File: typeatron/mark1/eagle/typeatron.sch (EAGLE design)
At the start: 24 parts

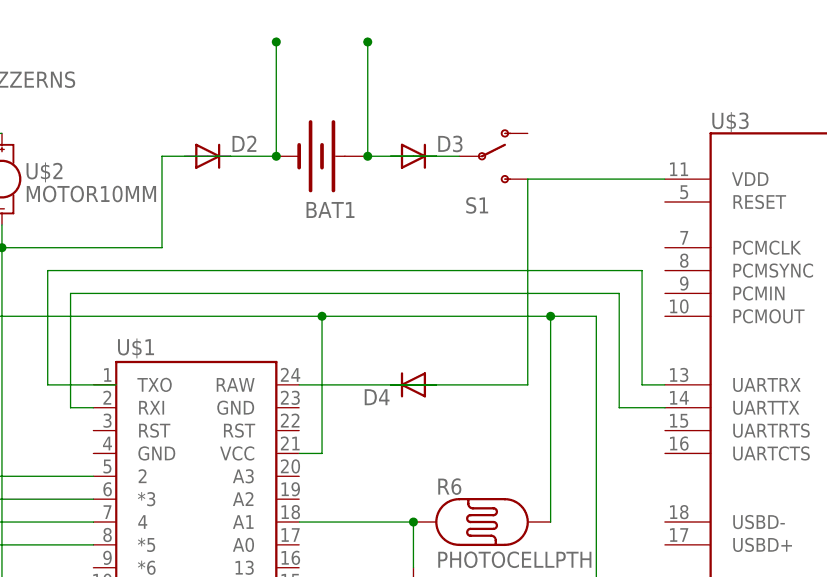
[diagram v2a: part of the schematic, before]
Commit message: Yet another diode revision; minimizes voltage drop by protecting the microcontroller and modem in parallel, while still blocking power from VIN, allowing the battery to charge, and making safe all combinations of USB cable dis/connected, charger dis/connected, power switch closed/open
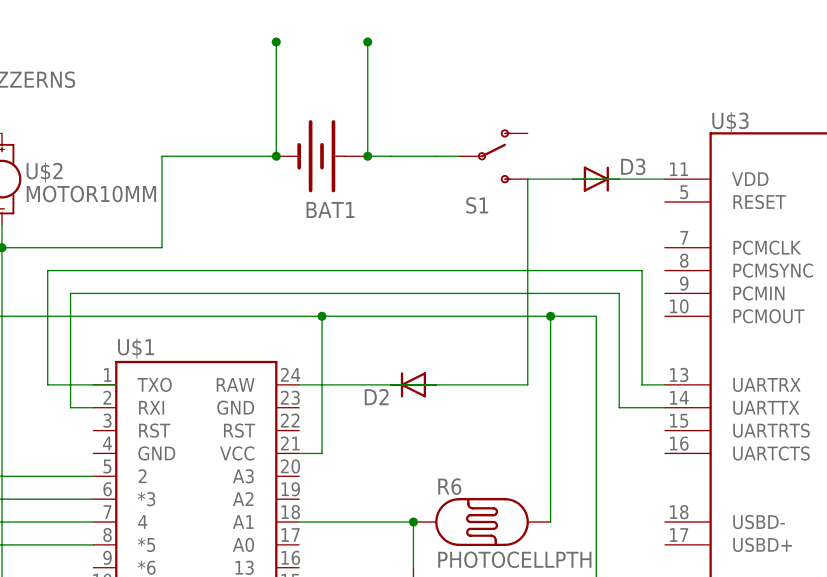
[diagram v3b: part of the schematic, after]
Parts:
- removed D4: (no value), SparkFun-DiscreteSemi:DIODEPTH
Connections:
- net N$10: now also D2.A, D2.C, D3.A, D3.C; no longer D4.A, D4.C
- net N$3: no longer D2.A, D2.C
- net N$9: no longer D3.A, D3.C
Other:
- moved on the sheet: D2, D3
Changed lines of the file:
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@@
 <part name="U1" library="SparkFun-Sensors" deviceset="MPU-9150" device="QFN-24-NP"/>
 <part name="R8" library="SparkFun-Resistors" deviceset="10KOHM1/6W5%(PTH)" device="KIT" value="10k"/>
+<part name="D2" library="SparkFun-DiscreteSemi" deviceset="DIODE" device="PTH"/>
 <part name="D3" library="SparkFun-DiscreteSemi" deviceset="DIODE" device="PTH"/>
-<part name="D2" library="SparkFun-DiscreteSemi" deviceset="DIODE" device="PTH"/>
-<part name="D4" library="SparkFun-DiscreteSemi" deviceset="DIODE" device="PTH"/>
 </parts>
 <sheets>
@@
 <instance part="U1" gate="G$1" x="53.34" y="5.08"/>
 <instance part="R8" gate="G$1" x="86.36" y="55.88" rot="R90"/>
-<instance part="D3" gate="G$1" x="86.36" y="106.68"/>
-<instance part="D2" gate="G$1" x="63.5" y="106.68"/>
-<instance part="D4" gate="G$1" x="86.36" y="81.28" rot="R180"/>
+<instance part="D2" gate="G$1" x="86.36" y="81.28" rot="R180"/>
+<instance part="D3" gate="G$1" x="106.68" y="104.14"/>
 </instances>
 <busses>
@@
 <pinref part="BAT1" gate="G$1" pin="+"/>
 <pinref part="S1" gate="1" pin="P"/>
-<wire x1="88.9" y1="106.68" x2="81.28" y2="106.68" width="0.1524" layer="91"/>
+<wire x1="83.82" y1="106.68" x2="81.28" y2="106.68" width="0.1524" layer="91"/>
 <wire x1="81.28" y1="119.38" x2="81.28" y2="106.68" width="0.1524" layer="91"/>
 <junction x="81.28" y="106.68"/>
-<pinref part="D3" gate="G$1" pin="A"/>
-<pinref part="D3" gate="G$1" pin="C"/>
 <wire x1="83.82" y1="106.68" x2="88.9" y2="106.68" width="0.1524" layer="91"/>
 <wire x1="88.9" y1="106.68" x2="91.44" y2="106.68" width="0.1524" layer="91"/>
@@
 <wire x1="83.82" y1="81.28" x2="99.06" y2="81.28" width="0.1524" layer="91"/>
 <wire x1="99.06" y1="81.28" x2="99.06" y2="104.14" width="0.1524" layer="91"/>
-<wire x1="99.06" y1="104.14" x2="114.3" y2="104.14" width="0.1524" layer="91"/>
+<wire x1="99.06" y1="104.14" x2="104.14" y2="104.14" width="0.1524" layer="91"/>
 <pinref part="U$3" gate="G$1" pin="VDD"/>
-<pinref part="D4" gate="G$1" pin="A"/>
-<pinref part="D4" gate="G$1" pin="C"/>
+<pinref part="D2" gate="G$1" pin="A"/>
+<pinref part="D2" gate="G$1" pin="C"/>
+<pinref part="D3" gate="G$1" pin="A"/>
+<wire x1="104.14" y1="104.14" x2="109.22" y2="104.14" width="0.1524" layer="91"/>
+<pinref part="D3" gate="G$1" pin="C"/>
+<wire x1="109.22" y1="104.14" x2="114.3" y2="104.14" width="0.1524" layer="91"/>
 </segment>
 </net>
@@
 <wire x1="71.12" y1="119.38" x2="71.12" y2="106.68" width="0.1524" layer="91"/>
 <junction x="71.12" y="106.68"/>
-<wire x1="71.12" y1="106.68" x2="66.04" y2="106.68" width="0.1524" layer="91"/>
-<wire x1="66.04" y1="106.68" x2="60.96" y2="106.68" width="0.1524" layer="91"/>
-<wire x1="60.96" y1="106.68" x2="58.42" y2="106.68" width="0.1524" layer="91"/>
+<wire x1="71.12" y1="106.68" x2="58.42" y2="106.68" width="0.1524" layer="91"/>
 <wire x1="58.42" y1="96.52" x2="58.42" y2="106.68" width="0.1524" layer="91"/>
 <junction x="40.64" y="96.52"/>
@@
 <wire x1="12.7" y1="15.24" x2="25.4" y2="15.24" width="0.1524" layer="91"/>
 <junction x="12.7" y="15.24"/>
-<pinref part="D2" gate="G$1" pin="A"/>
-<pinref part="D2" gate="G$1" pin="C"/>
 <junction x="71.12" y="119.38"/>
 </segment>

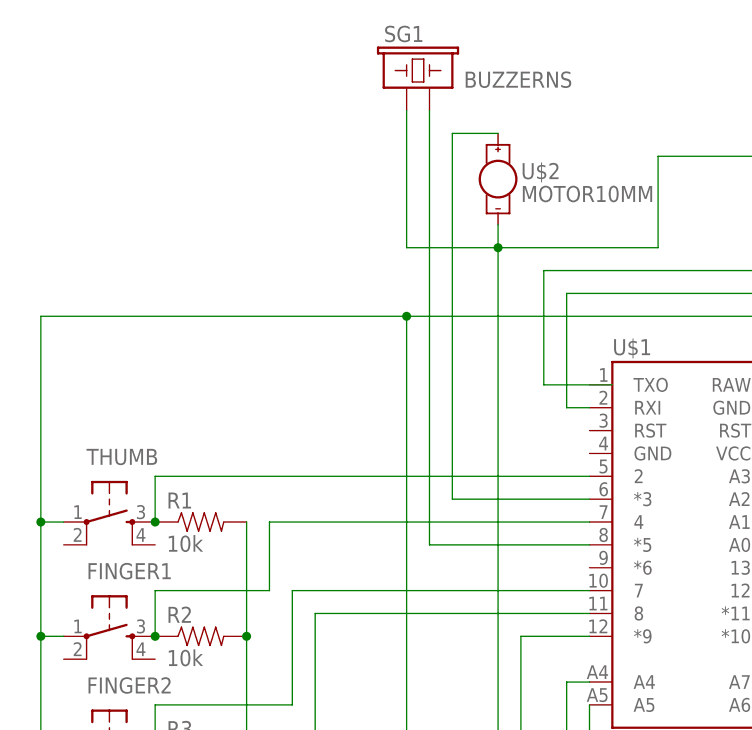
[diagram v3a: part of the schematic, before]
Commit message: Added the Typeatron's laser module
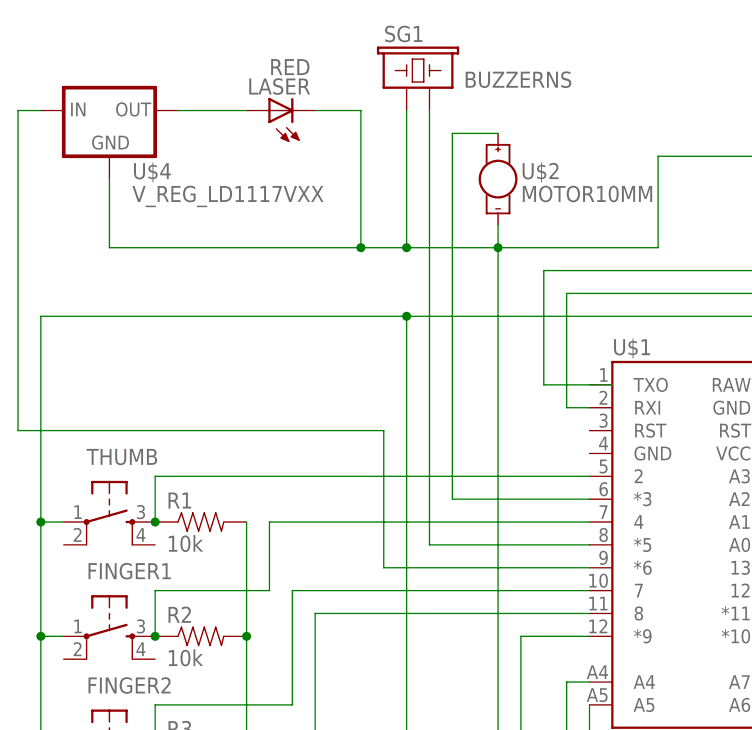
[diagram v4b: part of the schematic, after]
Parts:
- added LASER: RED, SparkFun-LED:LED-RED0603
- added U$4: V_REG_LD1117VXX, SparkFun-PowerIC:V_REG_LD1117VXX
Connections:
- new net N$19: LASER.A, U$4.OUT
- new net N$24: U$1.*6, U$4.IN
- net N$3: now also LASER.C, U$4.GND
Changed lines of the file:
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@@
 <part name="D2" library="SparkFun-DiscreteSemi" deviceset="DIODE" device="PTH"/>
 <part name="D3" library="SparkFun-DiscreteSemi" deviceset="DIODE" device="PTH"/>
+<part name="U$4" library="SparkFun-PowerIC" deviceset="V_REG_LD1117VXX" device=""/>
+<part name="LASER" library="SparkFun-LED" deviceset="LED-RED" device="0603" value="RED"/>
 </parts>
 <sheets>
@@
 <instance part="D2" gate="G$1" x="86.36" y="81.28" rot="R180"/>
 <instance part="D3" gate="G$1" x="106.68" y="104.14"/>
+<instance part="U$4" gate="G$1" x="-2.54" y="111.76"/>
+<instance part="LASER" gate="G$1" x="15.24" y="111.76" rot="R90"/>
 </instances>
 <busses>
@@
 <junction x="12.7" y="15.24"/>
 <junction x="71.12" y="119.38"/>
-</segment>
-</net>
+<pinref part="LASER" gate="G$1" pin="C"/>
+<wire x1="20.32" y1="111.76" x2="25.4" y2="111.76" width="0.1524" layer="91"/>
+<wire x1="25.4" y1="111.76" x2="25.4" y2="96.52" width="0.1524" layer="91"/>
+<wire x1="25.4" y1="96.52" x2="30.48" y2="96.52" width="0.1524" layer="91"/>
+<junction x="30.48" y="96.52"/>
+<pinref part="U$4" gate="G$1" pin="GND"/>
+<wire x1="-2.54" y1="104.14" x2="-2.54" y2="96.52" width="0.1524" layer="91"/>
+<wire x1="-2.54" y1="96.52" x2="25.4" y2="96.52" width="0.1524" layer="91"/>
+<junction x="25.4" y="96.52"/>
+</segment>
+</net>
+<net name="N$19" class="0">
+<segment>
+<pinref part="U$4" gate="G$1" pin="OUT"/>
+<pinref part="LASER" gate="G$1" pin="A"/>
+<wire x1="5.08" y1="111.76" x2="12.7" y2="111.76" width="0.1524" layer="91"/>
+</segment>
+</net>
+<net name="N$24" class="0">
+<segment>
+<pinref part="U$4" gate="G$1" pin="IN"/>
+<wire x1="-10.16" y1="111.76" x2="-12.7" y2="111.76" width="0.1524" layer="91"/>
+<wire x1="-12.7" y1="111.76" x2="-12.7" y2="76.2" width="0.1524" layer="91"/>
+<wire x1="-12.7" y1="76.2" x2="27.94" y2="76.2" width="0.1524" layer="91"/>
+<wire x1="27.94" y1="76.2" x2="27.94" y2="60.96" width="0.1524" layer="91"/>
+<pinref part="U$1" gate="G$1" pin="*6"/>
+<wire x1="27.94" y1="60.96" x2="50.8" y2="60.96" width="0.1524" layer="91"/>
+</segment>
+</net>

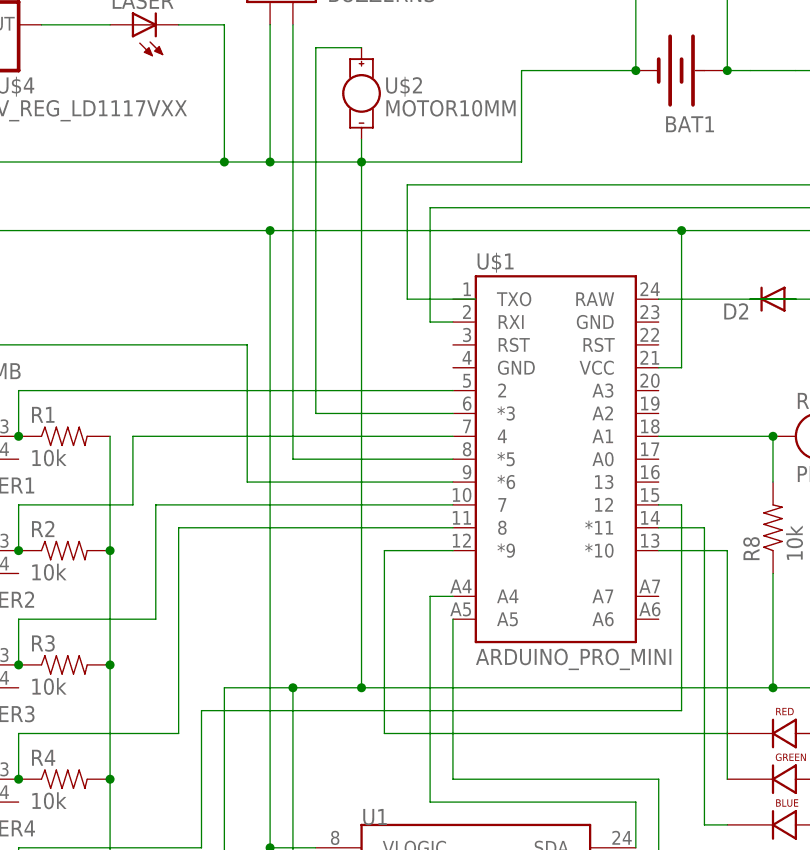
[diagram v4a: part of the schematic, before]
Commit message: Implemented the Typeatron's chording strategy in C/Arduino. However, SRAM limits the Duemilanove have already been reached. Chording logic likely to be moved to Java/Android.
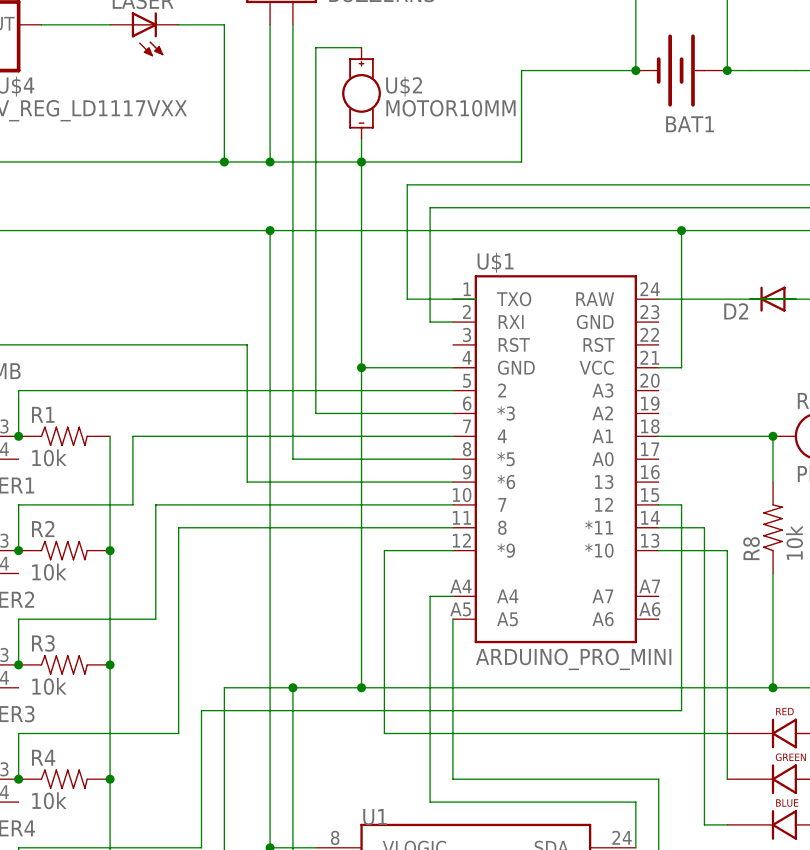
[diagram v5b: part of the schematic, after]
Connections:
- net N$3: now also U$1.GND
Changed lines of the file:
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@@
 <wire x1="40.64" y1="99.06" x2="40.64" y2="96.52" width="0.1524" layer="91"/>
 <junction x="40.64" y="38.1"/>
-<wire x1="40.64" y1="96.52" x2="40.64" y2="38.1" width="0.1524" layer="91"/>
+<wire x1="40.64" y1="96.52" x2="40.64" y2="73.66" width="0.1524" layer="91"/>
+<wire x1="40.64" y1="73.66" x2="40.64" y2="38.1" width="0.1524" layer="91"/>
 <wire x1="33.02" y1="2.54" x2="33.02" y2="38.1" width="0.1524" layer="91"/>
 <wire x1="86.36" y1="38.1" x2="157.48" y2="38.1" width="0.1524" layer="91"/>
@@
 <wire x1="-2.54" y1="96.52" x2="25.4" y2="96.52" width="0.1524" layer="91"/>
 <junction x="25.4" y="96.52"/>
+<pinref part="U$1" gate="G$1" pin="GND"/>
+<wire x1="50.8" y1="73.66" x2="40.64" y2="73.66" width="0.1524" layer="91"/>
+<junction x="40.64" y="73.66"/>
 </segment>
 </net>
